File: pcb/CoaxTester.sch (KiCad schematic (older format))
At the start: 14 parts

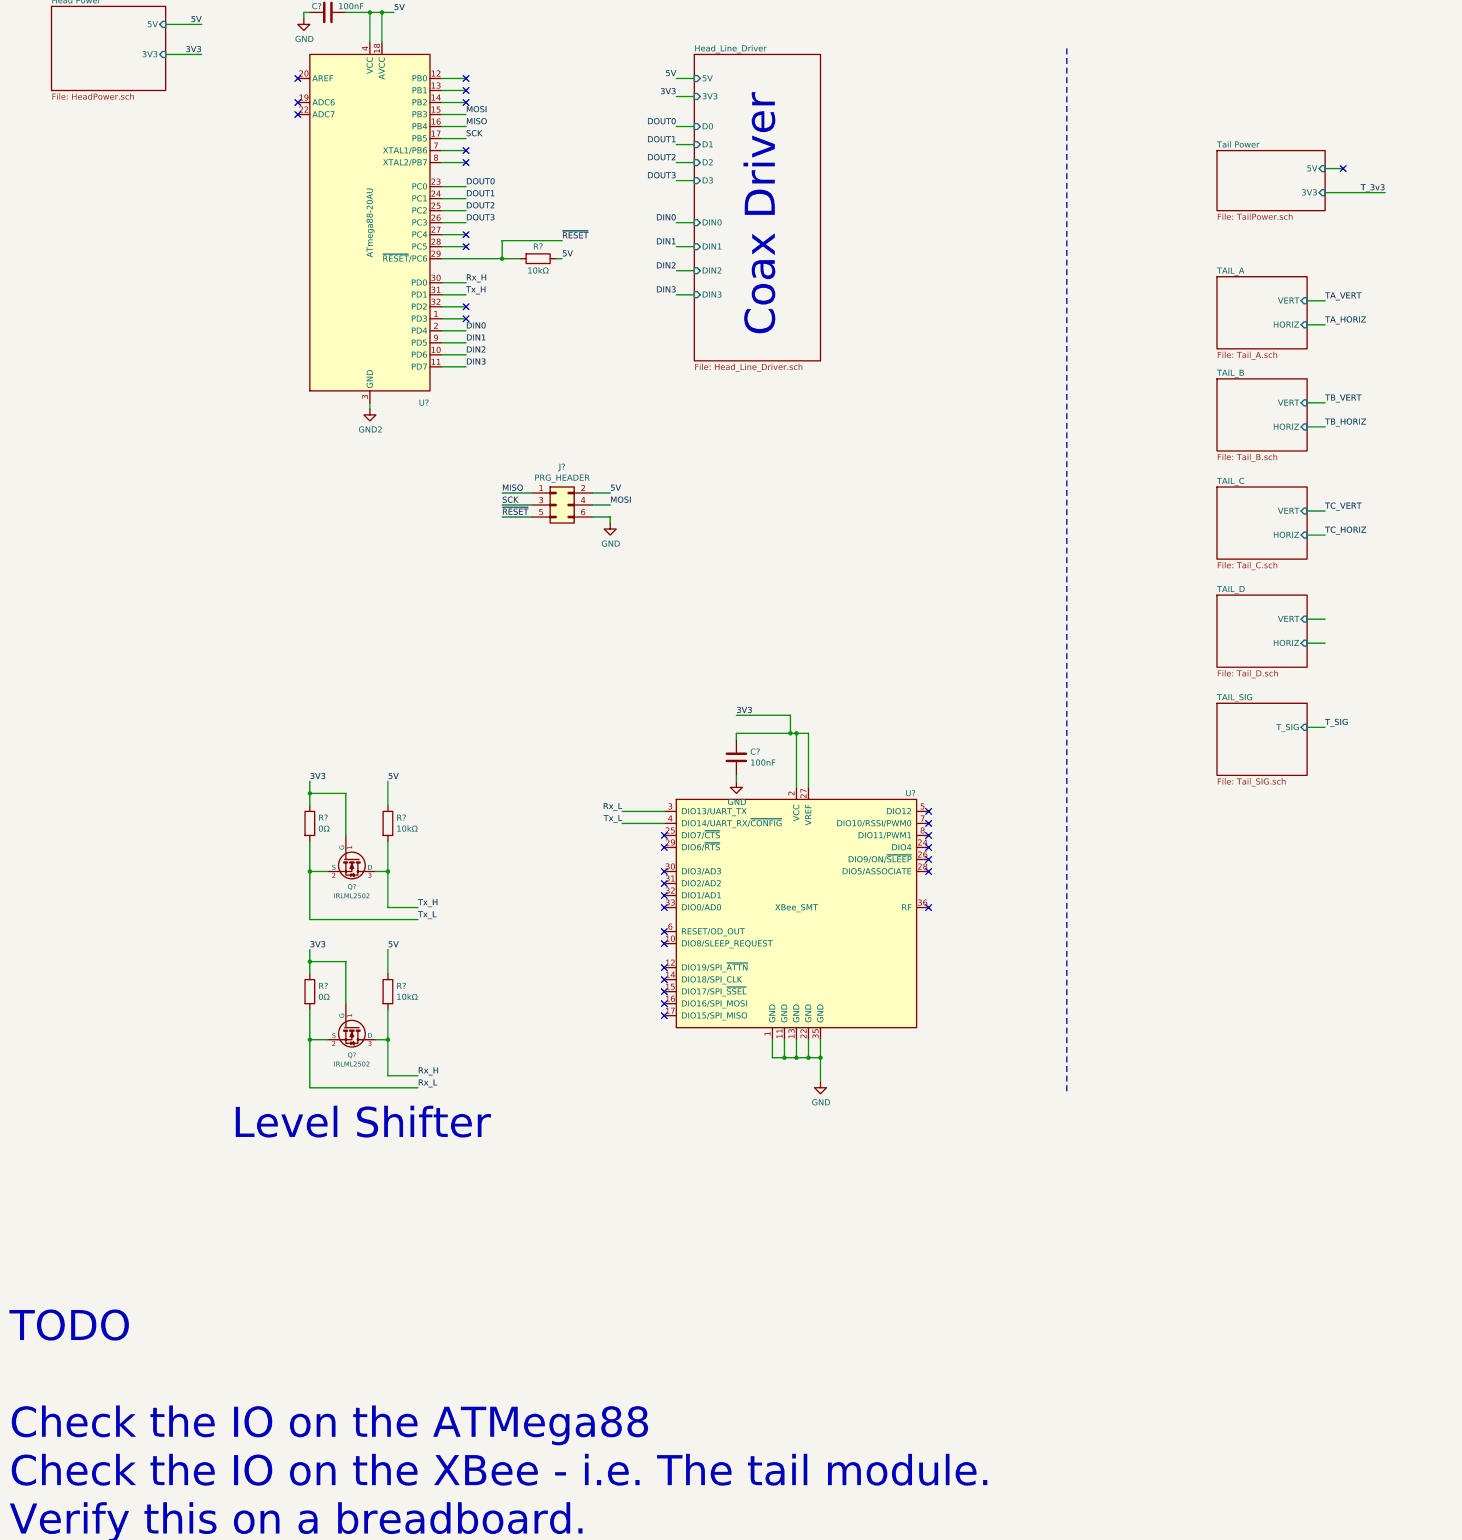
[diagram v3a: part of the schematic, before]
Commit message: Completes first cut of the schematic
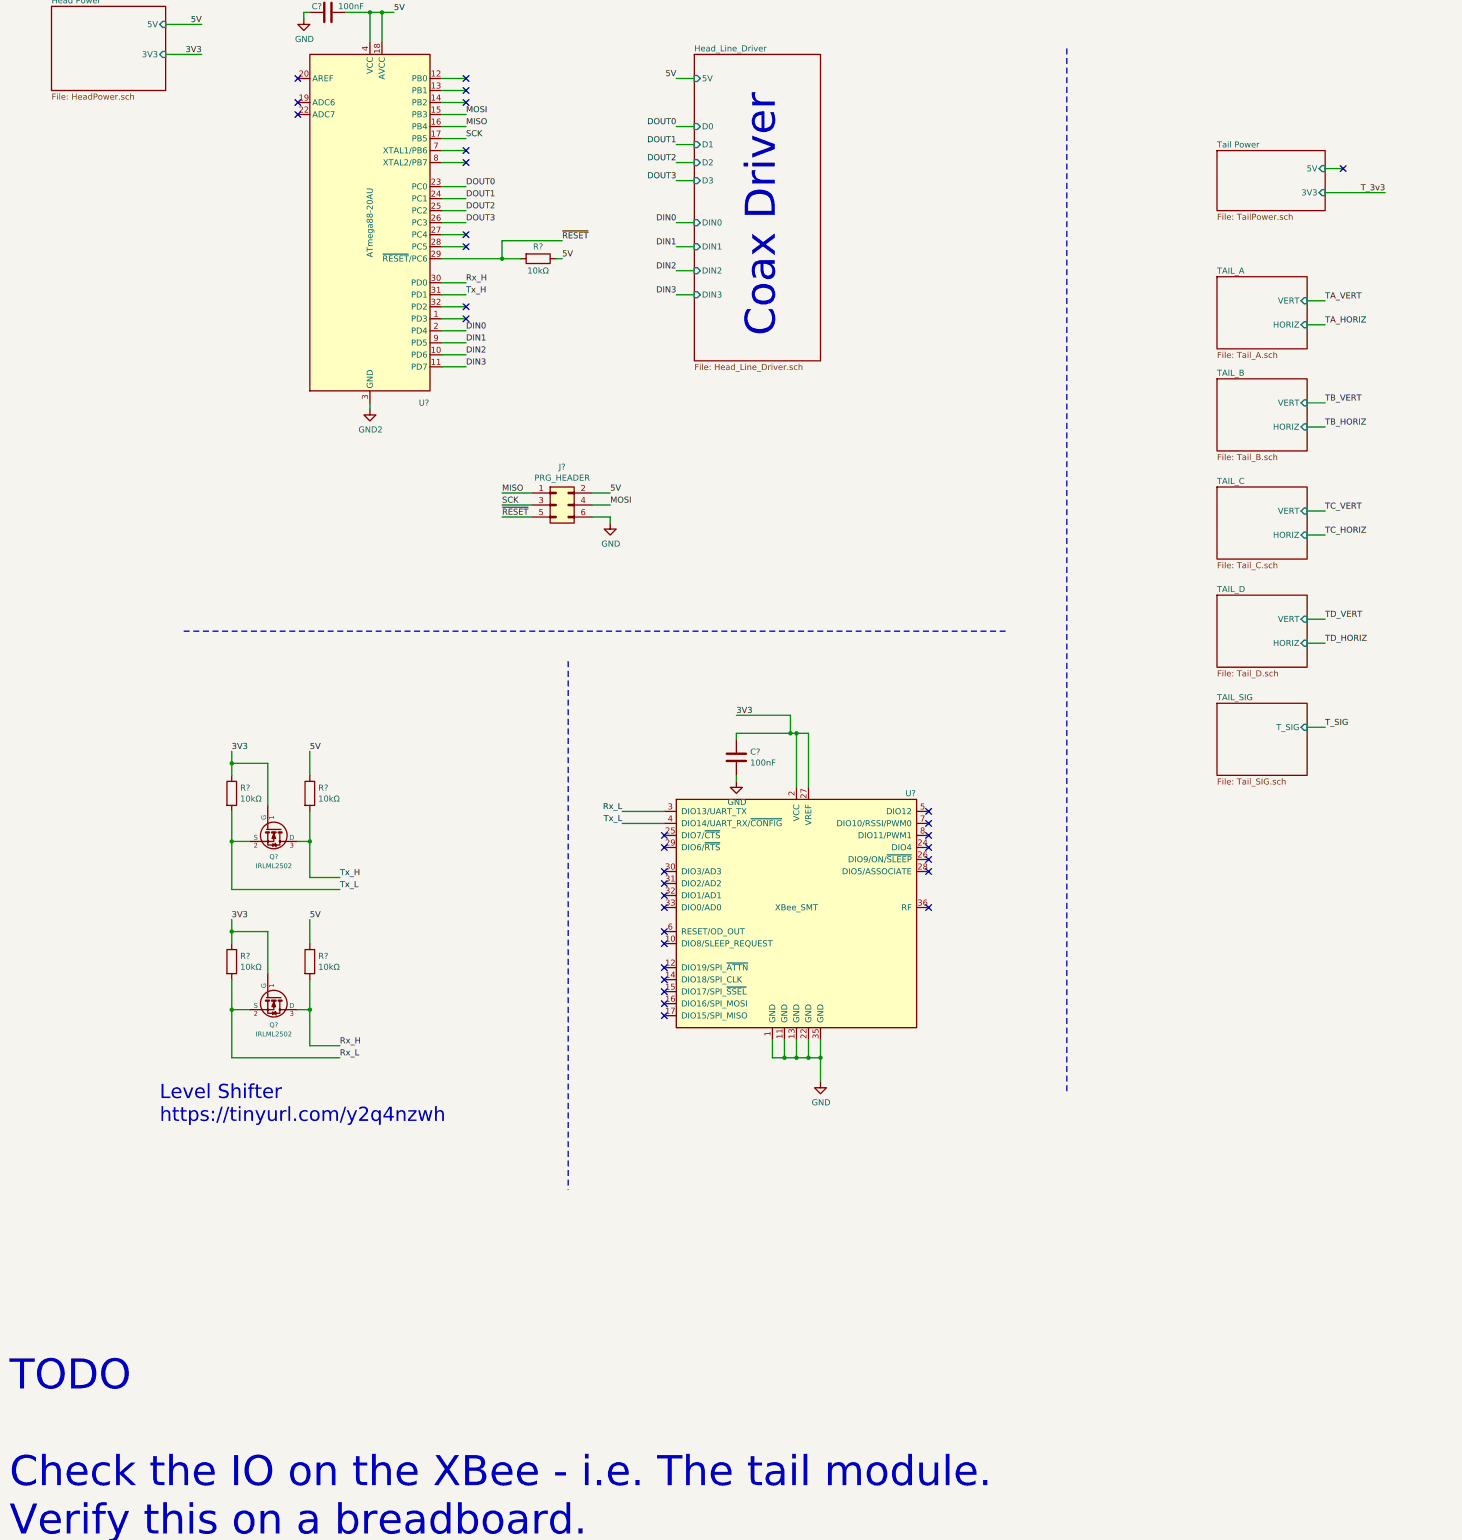
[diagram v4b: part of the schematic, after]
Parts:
- R? (x2): value 0Ω -> 10kΩ
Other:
- note added: "Level Shifter\nhttps://tinyurl.com/y2q4nzwh"
- note added: "TODO\n\nCheck the IO on the XBee - i.e. The tail module.\nVerify this on a breadboard."
- note removed: "Level Shifter"
- note removed: "TODO\n\nCheck the IO on the ATMega88\nCheck the IO on the XBee - i.e. The tail module.\nVerify this on a breadboard."
- moved on the sheet: Q?, R?
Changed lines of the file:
@@
 $EndComp
 Text Notes 250  13700 0    250  ~ 0
-TODO\n\nCheck the IO on the ATMega88\nCheck the IO on the XBee - i.e. The tail module.\nVerify this on a breadboard.
+TODO\n\nCheck the IO on the XBee - i.e. The tail module.\nVerify this on a breadboard.
 $Sheet
 S 600  950  950  700
@@
 F1 "Head_Line_Driver.sch" 50
 F2 "5V" I L 5950 1550 50
-F3 "3V3" I L 5950 1700 50
 F4 "D0" I L 5950 1950 50
 F5 "D1" I L 5950 2100 50
@@
 Wire Wire Line
 	5950 1550 5800 1550
-Wire Wire Line
-	5950 1700 5800 1700
 Text Label 5800 1550 2    50   ~ 0
 5V
-Text Label 5800 1700 2    50   ~ 0
-3V3
 Wire Wire Line
 	5950 1950 5800 1950
@@
 L Tfac-Symbols:IRLML2502 Q?
 U 1 1 61BF30EF
-P 3100 9450
-F 0 "Q?" V 3328 9450 40  0000 C CNN
-F 1 "IRLML2502" V 3404 9450 40  0000 C CNN
-F 2 "Micro3" H 2970 9552 29  0001 C CNN
-F 3 "" H 3100 9450 60  0000 C CNN
-	1    3100 9450
+P 2450 9200
+F 0 "Q?" V 2678 9200 40  0000 C CNN
+F 1 "IRLML2502" V 2754 9200 40  0000 C CNN
+F 2 "Micro3" H 2320 9302 29  0001 C CNN
+F 3 "" H 2450 9200 60  0000 C CNN
+	1    2450 9200
 	0    1    1    0
 $EndComp
@@
 L Device:R R?
 U 1 1 61BF465F
-P 2750 9150
-F 0 "R?" H 2820 9196 50  0000 L CNN
-F 1 "0Ω" H 2820 9105 50  0000 L CNN
-F 2 "Resistor_SMD:R_0805_2012Metric" V 2680 9150 50  0001 C CNN
-F 3 "~" H 2750 9150 50  0001 C CNN
-	1    2750 9150
+P 2100 8900
+F 0 "R?" H 2170 8946 50  0000 L CNN
+F 1 "10kΩ" H 2170 8855 50  0000 L CNN
+F 2 "Resistor_SMD:R_0805_2012Metric" V 2030 8900 50  0001 C CNN
+F 3 "~" H 2100 8900 50  0001 C CNN
+	1    2100 8900
 	1    0    0    -1
 $EndComp
@@
 L Device:R R?
 U 1 1 61BF6373
-P 3400 9150
-F 0 "R?" H 3470 9196 50  0000 L CNN
-F 1 "10kΩ" H 3470 9105 50  0000 L CNN
-F 2 "Resistor_SMD:R_0805_2012Metric" V 3330 9150 50  0001 C CNN
-F 3 "~" H 3400 9150 50  0001 C CNN
-	1    3400 9150
+P 2750 8900
+F 0 "R?" H 2820 8946 50  0000 L CNN
+F 1 "10kΩ" H 2820 8855 50  0000 L CNN
+F 2 "Resistor_SMD:R_0805_2012Metric" V 2680 8900 50  0001 C CNN
+F 3 "~" H 2750 8900 50  0001 C CNN
+	1    2750 8900
 	1    0    0    -1
 $EndComp
 Wire Wire Line
-	2750 8800 2750 8900
-Wire Wire Line
-	2750 9300 2750 9550
-Wire Wire Line
-	3400 8800 3400 9000
-Wire Wire Line
-	3400 9300 3400 9550
-Wire Wire Line
-	2750 9550 2900 9550
-Connection ~ 2750 9550
-Connection ~ 3400 9550
-Wire Wire Line
-	3400 9550 3400 9850
-Wire Wire Line
-	3300 9550 3400 9550
-Wire Wire Line
-	3050 9250 3050 8900
-Wire Wire Line
-	3050 8900 2750 8900
-Connection ~ 2750 8900
-Wire Wire Line
-	2750 8900 2750 9000
-Wire Wire Line
-	3400 9850 3650 9850
-Text Label 3650 9850 0    50   ~ 0
+	2100 8550 2100 8650
+Wire Wire Line
+	2100 9050 2100 9300
+Wire Wire Line
+	2750 8550 2750 8750
+Wire Wire Line
+	2750 9050 2750 9300
+Wire Wire Line
+	2100 9300 2250 9300
+Connection ~ 2100 9300
+Connection ~ 2750 9300
+Wire Wire Line
+	2750 9300 2750 9600
+Wire Wire Line
+	2650 9300 2750 9300
+Wire Wire Line
+	2400 9000 2400 8650
+Wire Wire Line
+	2400 8650 2100 8650
+Connection ~ 2100 8650
+Wire Wire Line
+	2100 8650 2100 8750
+Wire Wire Line
+	2750 9600 3000 9600
+Text Label 3000 9600 0    50   ~ 0
 Rx_H
-Text Label 2750 8800 0    50   ~ 0
+Text Label 2100 8550 0    50   ~ 0
 3V3
-Text Label 3400 8800 0    50   ~ 0
+Text Label 2750 8550 0    50   ~ 0
 5V
 Wire Wire Line
-	2750 9550 2750 9950
+	2100 9300 2100 9700
 $Comp
 L Tfac-Symbols:IRLML2502 Q?
 U 1 1 61C3D1AE
-P 3100 8050
-F 0 "Q?" V 3328 8050 40  0000 C CNN
-F 1 "IRLML2502" V 3404 8050 40  0000 C CNN
-F 2 "Micro3" H 2970 8152 29  0001 C CNN
-F 3 "" H 3100 8050 60  0000 C CNN
-	1    3100 8050
+P 2450 7800
+F 0 "Q?" V 2678 7800 40  0000 C CNN
+F 1 "IRLML2502" V 2754 7800 40  0000 C CNN
+F 2 "Micro3" H 2320 7902 29  0001 C CNN
+F 3 "" H 2450 7800 60  0000 C CNN
+	1    2450 7800
 	0    1    1    0
 $EndComp
@@
 L Device:R R?
 U 1 1 61C3D1B8
-P 2750 7750
-F 0 "R?" H 2820 7796 50  0000 L CNN
-F 1 "0Ω" H 2820 7705 50  0000 L CNN
-F 2 "Resistor_SMD:R_0805_2012Metric" V 2680 7750 50  0001 C CNN
-F 3 "~" H 2750 7750 50  0001 C CNN
-	1    2750 7750
+P 2100 7500
+F 0 "R?" H 2170 7546 50  0000 L CNN
+F 1 "10kΩ" H 2170 7455 50  0000 L CNN
+F 2 "Resistor_SMD:R_0805_2012Metric" V 2030 7500 50  0001 C CNN
+F 3 "~" H 2100 7500 50  0001 C CNN
+	1    2100 7500
 	1    0    0    -1
 $EndComp
@@
 L Device:R R?
 U 1 1 61C3D1C2
-P 3400 7750
-F 0 "R?" H 3470 7796 50  0000 L CNN
-F 1 "10kΩ" H 3470 7705 50  0000 L CNN
-F 2 "Resistor_SMD:R_0805_2012Metric" V 3330 7750 50  0001 C CNN
-F 3 "~" H 3400 7750 50  0001 C CNN
-	1    3400 7750
+P 2750 7500
+F 0 "R?" H 2820 7546 50  0000 L CNN
+F 1 "10kΩ" H 2820 7455 50  0000 L CNN
+F 2 "Resistor_SMD:R_0805_2012Metric" V 2680 7500 50  0001 C CNN
+F 3 "~" H 2750 7500 50  0001 C CNN
+	1    2750 7500
 	1    0    0    -1
 $EndComp
 Wire Wire Line
-	2750 7400 2750 7500
-Wire Wire Line
-	2750 7900 2750 8150
-Wire Wire Line
-	3400 7400 3400 7600
-Wire Wire Line
-	3400 7900 3400 8150
-Wire Wire Line
-	2750 8150 2900 8150
-Connection ~ 2750 8150
-Connection ~ 3400 8150
-Wire Wire Line
-	3400 8150 3400 8450
-Wire Wire Line
-	3300 8150 3400 8150
-Wire Wire Line
-	3050 7850 3050 7500
-Wire Wire Line
-	3050 7500 2750 7500
-Connection ~ 2750 7500
-Wire Wire Line
-	2750 7500 2750 7600
-Wire Wire Line
-	3400 8450 3650 8450
-Text Label 3650 8450 0    50   ~ 0
+	2100 7150 2100 7250
+Wire Wire Line
+	2100 7650 2100 7900
+Wire Wire Line
+	2750 7150 2750 7350
+Wire Wire Line
+	2750 7650 2750 7900
+Wire Wire Line
+	2100 7900 2250 7900
+Connection ~ 2100 7900
+Connection ~ 2750 7900
+Wire Wire Line
+	2750 7900 2750 8200
+Wire Wire Line
+	2650 7900 2750 7900
+Wire Wire Line
+	2400 7600 2400 7250
+Wire Wire Line
+	2400 7250 2100 7250
+Connection ~ 2100 7250
+Wire Wire Line
+	2100 7250 2100 7350
+Wire Wire Line
+	2750 8200 3000 8200
+Text Label 3000 8200 0    50   ~ 0
 Tx_H
-Text Label 3650 8550 0    50   ~ 0
+Text Label 3000 8300 0    50   ~ 0
 Tx_L
-Text Label 2750 7400 0    50   ~ 0
+Text Label 2100 7150 0    50   ~ 0
 3V3
-Text Label 3400 7400 0    50   ~ 0
+Text Label 2750 7150 0    50   ~ 0
 5V
 Wire Wire Line
-	2750 8550 3650 8550
-Wire Wire Line
-	2750 8150 2750 8550
+	2100 8300 3000 8300
+Wire Wire Line
+	2100 7900 2100 8300
 Wire Wire Line
 	4350 3050 4350 2900
@@
 	4350 3050 4500 3050
 Wire Wire Line
-	2750 9950 3650 9950
-Text Label 3650 9950 0    50   ~ 0
+	2100 9700 3000 9700
+Text Label 3000 9700 0    50   ~ 0
 Rx_L
 Wire Wire Line
@@
 	1    0    0    -1
 $EndComp
-Text Notes 2100 10400 0    250  ~ 0
-Level Shifter
+Text Notes 1500 10250 0    118  ~ 0
+Level Shifter\nhttps://tinyurl.com/y2q4nzwh
 Text Notes 6650 3700 1    250  ~ 0
 Coax Driver
+Wire Notes Line
+	1700 6150 8550 6150
+Wire Notes Line
+	4900 6400 4900 10800
+Text Label 11200 6050 0    50   ~ 0
+TD_VERT
+Text Label 11200 6250 0    50   ~ 0
+TD_HORIZ
 $EndSCHEMATC
